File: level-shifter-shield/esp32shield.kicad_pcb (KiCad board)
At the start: 2 copper layers, 83 x 71 mm, 56 parts, among them J1 Power_Terminal, J10 Screw_Terminal_01x02, J11 Screw_Terminal_01x02, J12 Screw_Terminal_01x02, J2 Conn_01x19_Pin, J3 Power_Terminal, J4 Conn_01x19_Socket, J5 Power_Terminal, J6 Conn_01x19_Socket, J7 Conn_01x19_Pin, J8 Power_Terminal, J9 Screw_Terminal_01x02, U1 LM7805, U2 IXDD604PI, U3 IXDD604PI, U4 IXDD604PI, U5 IXDD604PI

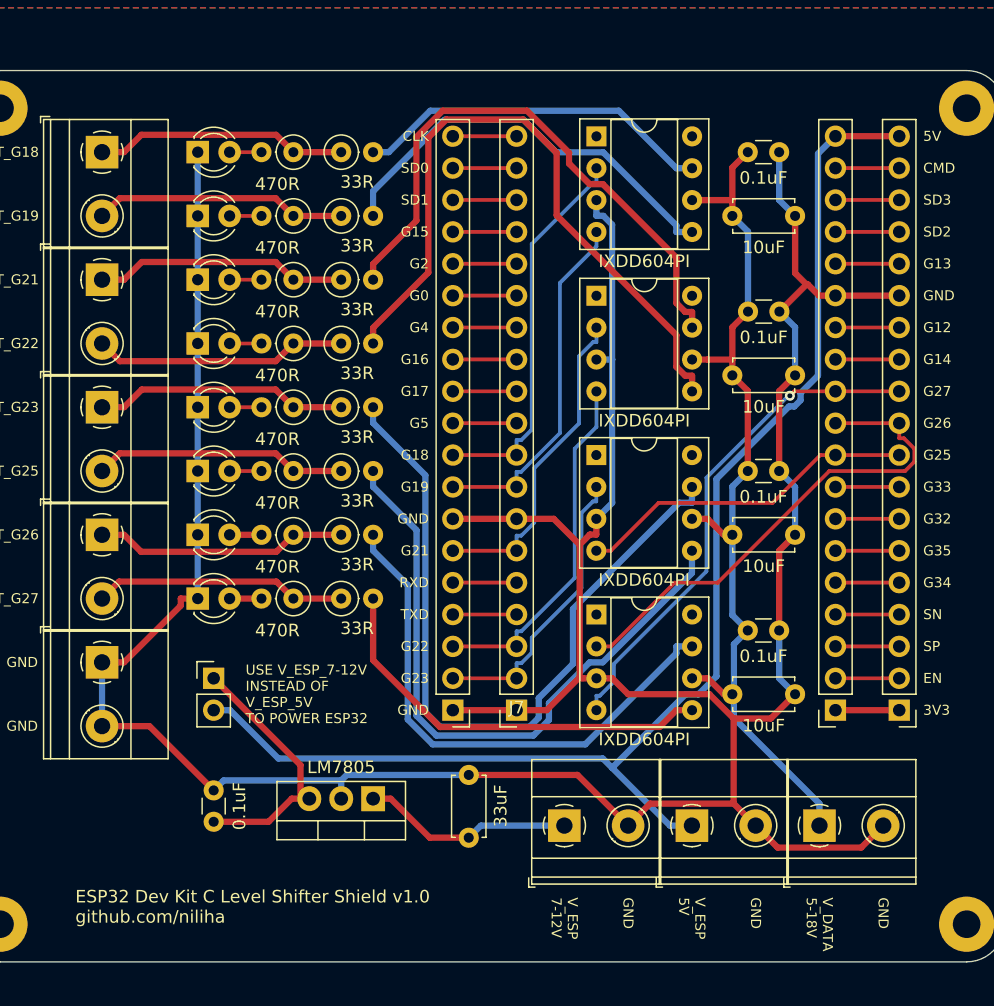
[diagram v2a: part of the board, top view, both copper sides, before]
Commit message: Add production files for level shifter shield
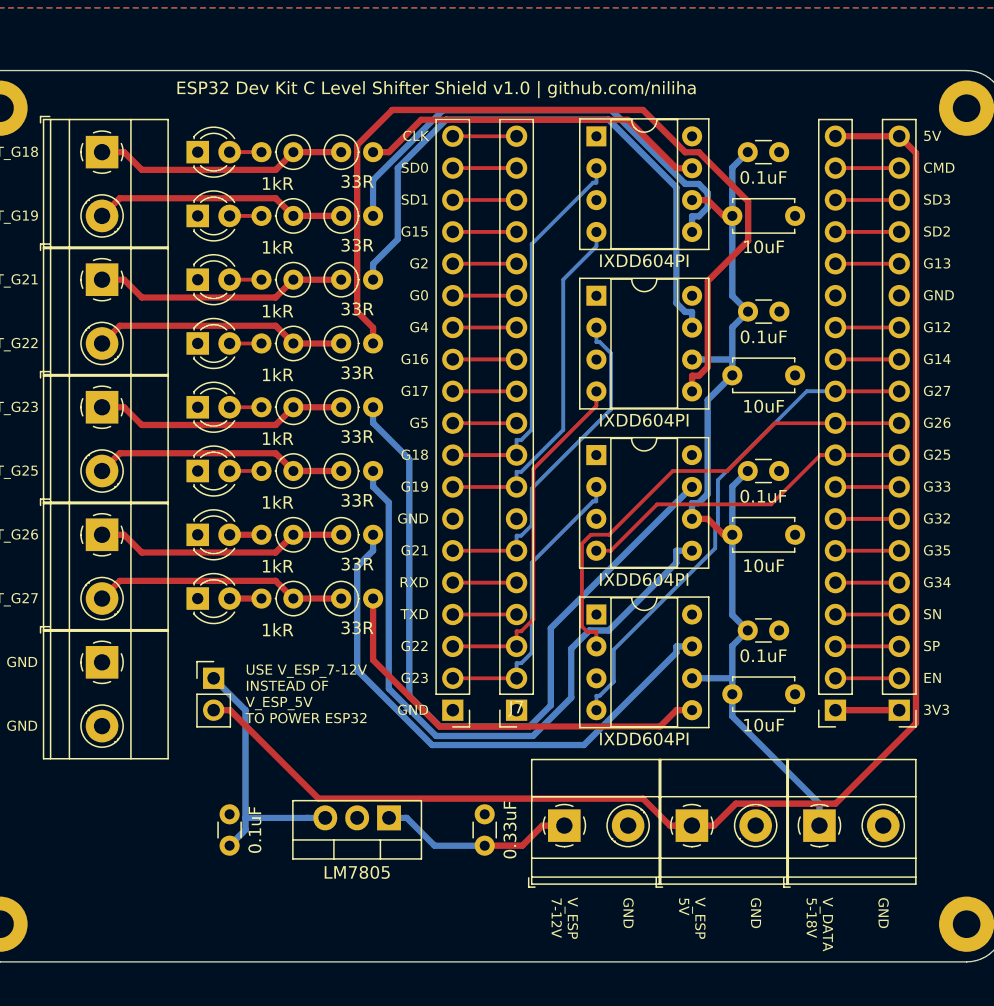
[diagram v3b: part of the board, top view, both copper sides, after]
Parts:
- C1: value 33uF -> 0.33uF; footprint Capacitor_THT:C_Disc_D4.7mm_W2.5mm_P5.00mm -> Capacitor_THT:C_Disc_D3.0mm_W1.6mm_P2.50mm
- R10, R11, R12, R13, R14, R15, R16, R9: value 470R -> 1kR
- moved C2 2.29 mm to (161.3, 118.7)
- moved U1 1.99 mm to (174.0, 116.5)
- moved C1 1.42 mm to (181.6, 118.7)
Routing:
- net GND: track 266.7 -> 0.00 mm
- net /OUT_G22: track 53.9 -> 69.0 mm
- net V_ESP_5V: track 105.5 -> 115.5 mm
- net V_DATA: track 74.0 -> 78.9 mm
- net /OUT_G19: track 33.7 -> 38.5 mm
- net /G26: track 40.3 -> 38.3 mm
- net /OUT_G21: track 46.1 -> 47.7 mm
- net V_ESP_7-12V: track 16.9 -> 15.5 mm
- net /OUT_G26: track 42.9 -> 44.0 mm
- net /OUT_G25: track 51.4 -> 52.5 mm
- net /G21: track 25.9 -> 26.8 mm
- net /G27: track 40.5 -> 39.9 mm, vias 1 -> 0
- net /OUT_G23: track 59.9 -> 59.2 mm
- net /OUT_G18: track 28.7 -> 28.1 mm
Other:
- board text added: "ESP32 Dev Kit C Level Shifter Shield v1.0 | github.com/niliha"
- board text removed: "ESP32 Dev Kit C Level Shifter Shield v1.0 github.com/niliha"
